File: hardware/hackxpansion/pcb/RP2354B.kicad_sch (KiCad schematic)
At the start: 34 parts, among them J1 Conn_01x03_MountingPin, SW1 SW_Push, SW2 SW_Push, U2 RP2354B, Y1 ABM8-272-T3

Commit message: changed bom, added v cut
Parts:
- C15, C16: LCSC C52923 -> C23733
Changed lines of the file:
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@@
 			)
 		)
-		(property "LCSC" "C52923"
+		(property "LCSC" "C23733"
 			(at 31.75 59.69 0)
 			(hide yes)
@@
 			)
 		)
-		(property "LCSC" "C52923"
+		(property "LCSC" "C23733"
 			(at 40.64 66.04 0)
 			(hide yes)

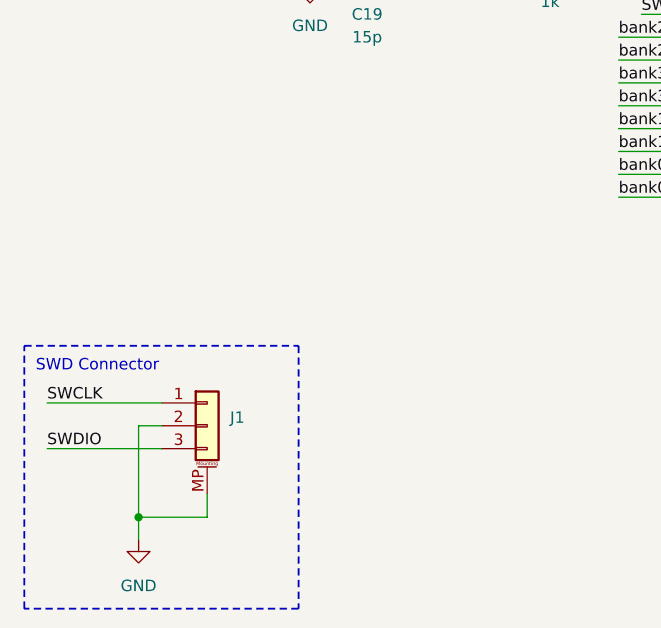
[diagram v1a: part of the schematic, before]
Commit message: updated debug connector to standard 2x5 1.27mm
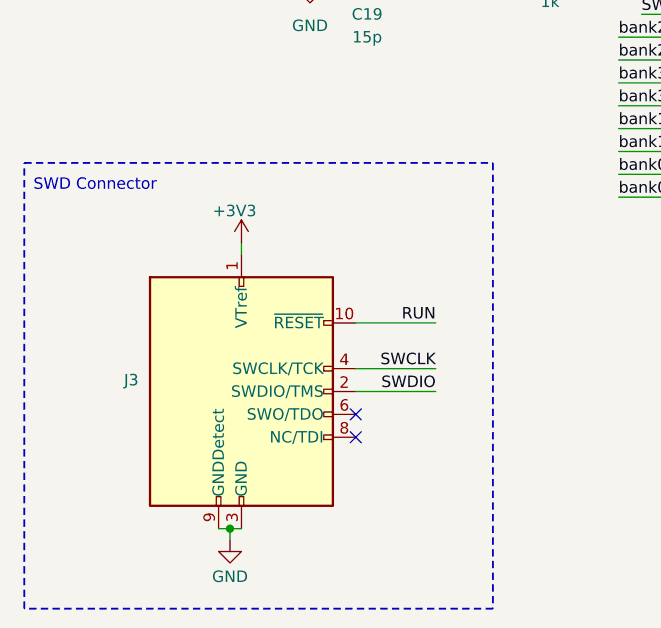
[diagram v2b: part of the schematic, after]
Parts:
- removed J1: Conn_01x03_MountingPin, Connector_JST:JST_SH_SM03B-SRSS-TB_1x03-1MP_P1.00mm_Horizontal, symbol Connector_Generic_MountingPin:Conn_01x03_MountingPin
- added J3: Conn_ARM_JTAG_SWD_10, Connector_PinHeader_1.27mm:PinHeader_2x05_P1.27mm_Vertical_SMD, symbol Connector:Conn_ARM_JTAG_SWD_10
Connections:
- net +3V3: now also J3.1 (VTref)
- net GND: now also J3.3 (GND), J3.5 (GND), J3.9 (GNDDetect)
- net RUN: now also J3.10 (~{RESET})
- net SWCLK: now also J3.4 (SWCLK/TCK)
- net SWDIO: now also J3.2 (SWDIO/TMS)
- no-connect marks 0 -> 2
